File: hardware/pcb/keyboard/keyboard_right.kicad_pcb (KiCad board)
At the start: 2 copper layers, 133.8 x 110.4 mm, 108 parts, among them J1 SM04B-SRSS-TB, J2 PJ320D, J3 HRO_TYPE-C-31-M-12, J4 FH34SRJ-10S-0.5SH, SW29 PTS845, U1 74HC4051, U2 OPA350UA, U3 DT1446-04S, U4 XC6220B331MR-G, U5 STM32G0B1KETx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

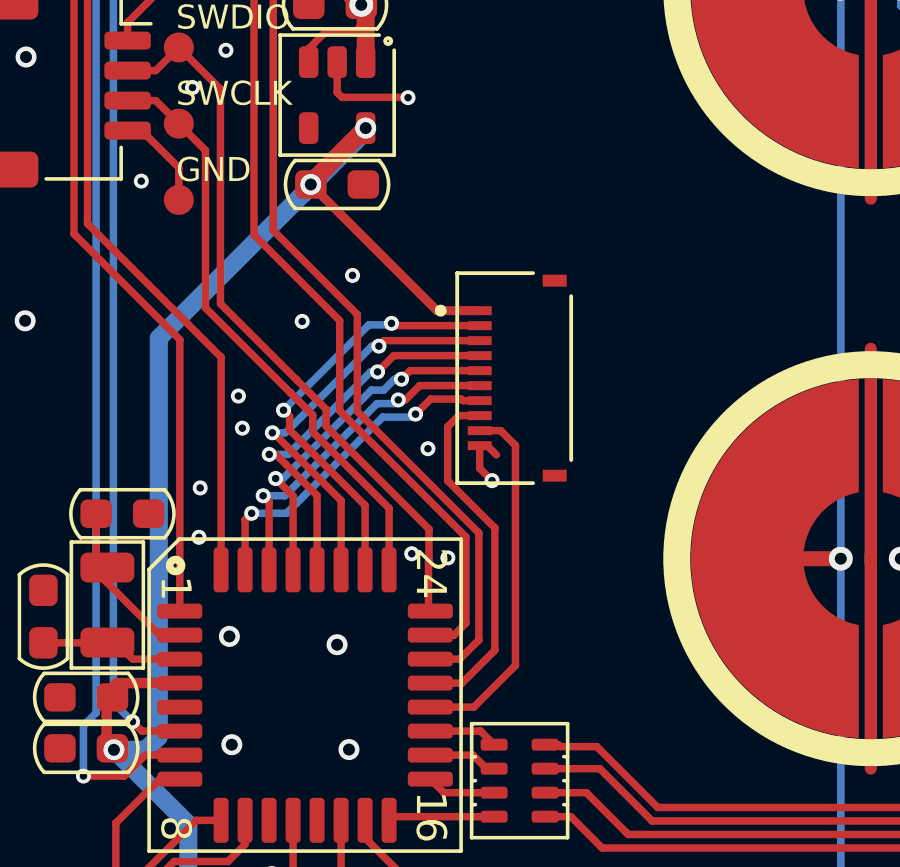
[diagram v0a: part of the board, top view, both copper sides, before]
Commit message: roate FFC Connector
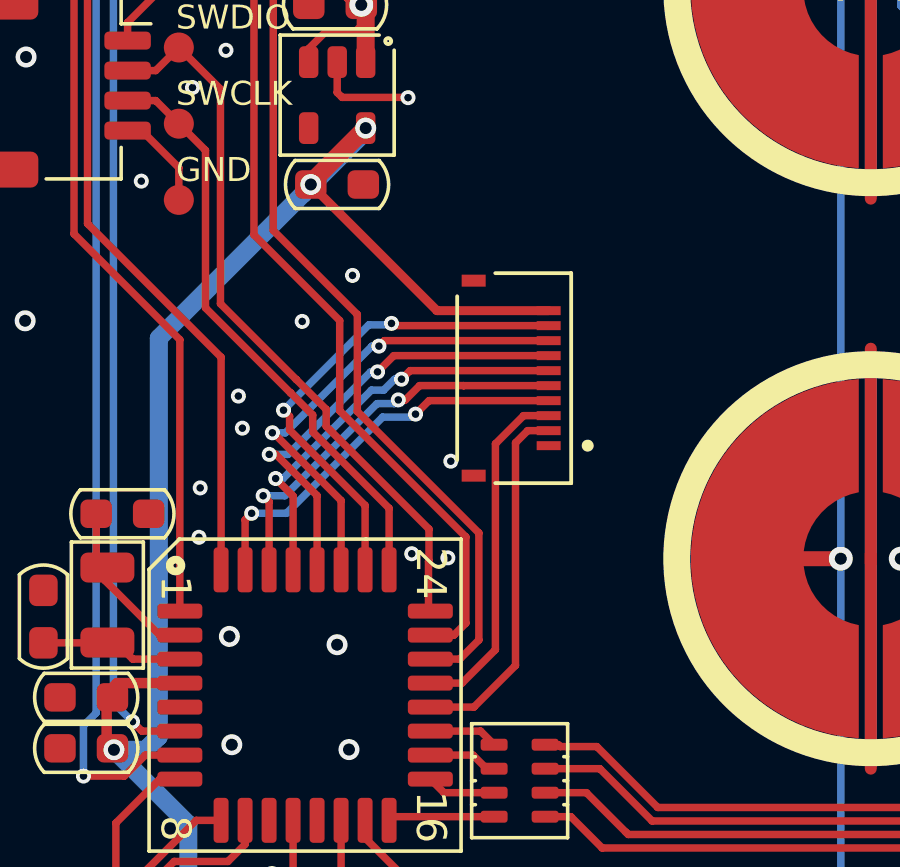
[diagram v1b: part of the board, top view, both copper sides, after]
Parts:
- turned J4 to -90 degrees
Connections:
- J4 pad 1: +3V3 -> GND
- J4 pad 10: GND -> +3V3
- J4 pad 2: ACCS_1 -> ACCS_8
- J4 pad 3: ACCS_2 -> ACCS_7
- J4 pad 4: ACCS_3 -> ACCS_6
- J4 pad 5: ACCS_4 -> ACCS_5
- J4 pad 6: ACCS_5 -> ACCS_4
- J4 pad 7: ACCS_6 -> ACCS_3
- J4 pad 8: ACCS_7 -> ACCS_2
- J4 pad 9: ACCS_8 -> ACCS_1
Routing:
- net ACCS_5: track 11.3 -> 13.6 mm
- net ACCS_4: track 11.6 -> 13.9 mm
- net ACCS_1: track 14.2 -> 16.5 mm
- net +3V3: track 68.9 -> 71.2 mm
- net ACCS_2: track 13.7 -> 16.0 mm
- net ACCS_3: track 13.0 -> 15.3 mm
- net ACCS_6: track 11.2 -> 13.4 mm
- net GND: track 15.1 -> 13.3 mm, vias 45 -> 44

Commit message: Right init
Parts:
- removed R4: 10k, PCM_Resistor_SMD_AKL:R_0603_1608Metric_Pad0.98x0.95mm
- removed R5: 5.6k, PCM_Resistor_SMD_AKL:R_0603_1608Metric_Pad0.98x0.95mm
- added C11: 4.7 uF, PCM_Capacitor_SMD_AKL:C_0603_1608Metric, F.Cu at (86.5, 89.7)
- added C12: 1u, PCM_Capacitor_SMD_AKL:C_0603_1608Metric, F.Cu at (85.4, 91.6)
- added C13: 10n, PCM_Capacitor_SMD_AKL:C_0603_1608Metric, F.Cu at (85.4, 94.0)
- added FB1: 1kΩ 100mhz, Inductor_SMD:L_0603_1608Metric, F.Cu at (87.7, 92.3)
- added R1: 10k, PCM_Resistor_SMD_AKL:R_0603_1608Metric, F.Cu at (74.5, 85.7)
- C10, C2, C3, C4, C6, C7: footprint PCM_Capacitor_SMD_AKL:C_0603_1608Metric_Pad1.05x0.95mm -> PCM_Capacitor_SMD_AKL:C_0603_1608Metric
- C5: value 4.7u -> 0.1uF; footprint PCM_Capacitor_SMD_AKL:C_0603_1608Metric_Pad1.05x0.95mm -> PCM_Capacitor_SMD_AKL:C_0603_1608Metric
- G19, H13, H14, H15, H16: moved to B.Cu
- J4: value FH34SRJ-10S-0.5SH -> Conn_01x12_MountingPin; footprint ec_parts:HRS_FH34SRJ-10S-0.5SH(50) -> ec_parts:HRS_FH34SRJ-12S-0.5SH(50)
- R6, R7: footprint PCM_Resistor_SMD_AKL:R_0603_1608Metric_Pad0.98x0.95mm -> PCM_Resistor_SMD_AKL:R_0603_1608Metric
- U5: value STM32G0B1KETx -> STM32G431KBTx; footprint PCM_Package_QFP_AKL:LQFP-32_7x7mm_P0.8mm -> Package_QFP:LQFP-32_7x7mm_P0.8mm
- Y1: value 32.768kHz -> 8MHz; footprint PCM_Crystal_AKL:Crystal_SMD_3215-2Pin_3.2x1.5mm -> PCM_Crystal_Handsoldering_AKL:Crystal_SMD_2520-4Pin_2.5x2.0mm
- moved H16 17.2 mm to (72.5, 102.7)
- moved H13 17.1 mm to (88.2, 102.7)
- moved H15 16.8 mm to (72.5, 55.6)
- moved H14 16.7 mm to (88.2, 55.6)
- moved C7 9.48 mm to (72.8, 85.7), turned to 90 degrees
- moved C6 7.28 mm to (73.8, 80.0), turned to 0 degrees
- moved C2 6.68 mm to (77.3, 93.1)
- moved C3 6.68 mm to (75.2, 108.1)
- moved H12 6.68 mm to (110.0, 129.2)
- moved C9 6.68 mm to (82.2, 68.5), turned to 180 degrees
- moved F1 6.68 mm to (86.2, 43.5)
- moved J1 6.68 mm to (73.2, 65.2)
- moved L1 6.68 mm to (86.4, 40.8)
- moved SW5 6.68 mm to (176.0, 64.4)
- moved TP1 6.68 mm to (76.9, 61.4)
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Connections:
- C6 pad 2: /OSC32_IN -> Net-(U5-PF0)
- C7 pad 2: /OSC32_OUT -> Net-(U5-PF1)
- D1 pad 2: Net-(D1-A) -> VBUS
- F1 pad 1: Net-(D1-A) -> VBUS
- F1 pad 2: VBUS -> Net-(F1-Pad2)
- J1 pad 1: +5V -> +3V3
- J3 pad A4: VBUS -> Net-(F1-Pad2)
- J3 pad A9: VBUS -> Net-(F1-Pad2)
- J3 pad B4: VBUS -> Net-(F1-Pad2)
- J3 pad B9: VBUS -> Net-(F1-Pad2)
- J4 pad 10: +3V3 -> unconnected-(J4-Pin_10-Pad10)
- J4 pad 2: ACCS_8 -> ACCS_7
- J4 pad 3: ACCS_7 -> ACCS_6
- J4 pad 4: ACCS_6 -> ACCS_5
- J4 pad 5: ACCS_5 -> ACCS_4
- J4 pad 6: ACCS_4 -> ACCS_3
- J4 pad 7: ACCS_3 -> ACCS_2
- J4 pad 8: ACCS_2 -> ACCS_1
- J4 pad 9: ACCS_1 -> +3V3
- TP1 pad 1: +5V -> +3V3
- U5 pad 1: USART_RX -> +3V3
- U5 pad 10: CSEL2 -> CSEL1
- U5 pad 11: /ADC1_IN4 -> CSEL2
- U5 pad 13: /ADC1_IN6 -> CHARGE_RST
- U5 pad 14: CHARGE_RST -> GND
- U5 pad 15: CSEL_EN -> VDDA
- U5 pad 16: TX3 -> GND
- U5 pad 17: TX2 -> +3V3
- U5 pad 18: TX1 -> TX3
- U5 pad 19: TX0 -> TX2
- U5 pad 2: /OSC32_IN -> Net-(U5-PF0)
- U5 pad 20: ACCS_8 -> TX1
- U5 pad 21: ACCS_7 -> D-
- U5 pad 22: D- -> D+
- U5 pad 23: D+ -> SWDIO
- U5 pad 24: SWDIO -> SWCLK
- U5 pad 25: SWCLK -> TX0
- U5 pad 26: ACCS_1 -> ACCS_2
- U5 pad 27: ACCS_2 -> ACCS_3
- U5 pad 28: ACCS_3 -> ACCS_4
- U5 pad 29: ACCS_4 -> ACCS_5
- U5 pad 3: /OSC32_OUT -> Net-(U5-PF1)
- U5 pad 30: ACCS_5 -> ACCS_6
- U5 pad 31: ACCS_6 -> ACCS_7
- U5 pad 32: USART_TX -> GND
- U5 pad 4: +3V3 -> /NRST
- U5 pad 5: GND -> ACCS_1
- U5 pad 6: /NRST -> CSEL_EN
- U5 pad 7: VBUS_DEC -> USART_TX
- U5 pad 8: CSEL0 -> USART_RX
- U5 pad 9: CSEL1 -> CSEL0
- Y1 pad 1: /OSC32_IN -> Net-(U5-PF1)
- Y1 pad 2: /OSC32_OUT -> GND
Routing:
- net VBUS_DEC: track 52.9 -> 0.00 mm, vias 4 -> 0
- net +3V3: track 71.2 -> 109.9 mm, vias 5 -> 9
- net GND: track 13.3 -> 33.4 mm, vias 44 -> 38
- net Net-(F1-Pad2): track 0.00 -> 17.2 mm, vias 0 -> 2
- net ACCS_8: track 12.7 -> 0.00 mm
- net VBUS: track 17.2 -> 29.5 mm, vias 2 -> 0
- net CSEL_EN: track 17.3 -> 29.0 mm, vias 0 -> 2
- net +5V: track 38.3 -> 27.5 mm, vias 2 -> 0
- net VDDA: track 0.00 -> 6.74 mm
- net Net-(U5-PF1): track 0.00 -> 5.62 mm
- net ACCS_1: track 16.5 -> 22.0 mm
- net USART_RX: track 40.8 -> 45.5 mm, vias 0 -> 2
- net ACCS_2: track 16.0 -> 11.4 mm
- net /OSC32_IN: track 4.50 -> 0.00 mm
- net Net-(D1-A): track 4.46 -> 0.00 mm
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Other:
- outline, holes or cut-outs redrawn
- board text added: "SWC"
- board text added: "SWD"
- board text removed: "SWCLK"
- board text removed: "SWDIO"

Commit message: usb hib init
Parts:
- added R4: 10k, PCM_Resistor_SMD_AKL:R_0603_1608Metric, F.Cu at (87.8, 66.9)
- added R5: 5.1k, PCM_Resistor_SMD_AKL:R_0603_1608Metric, F.Cu at (87.8, 65.1)
- added R8: 1k, PCM_Resistor_SMD_AKL:R_0603_1608Metric, F.Cu at (87.8, 68.6)
- J4: value Conn_01x12_MountingPin -> HRS_FH34SRJ-12S-0.5SH_50_
- moved H14 0.41 mm to (88.2, 55.2)
- moved H15 0.41 mm to (72.5, 55.2)
- moved C8 0.25 mm to (82.4, 62.5)
- moved C9 0.19 mm to (82.4, 68.5)
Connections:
- U5 pad 5: ACCS_1 -> CSEL0
- U5 pad 9: CSEL0 -> ACCS_1
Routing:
- net ACCS_3: track 11.9 -> 23.2 mm
- net ACCS_1: track 22.0 -> 33.3 mm
- net CSEL_EN: track 29.0 -> 24.4 mm
- net CSEL0: track 20.3 -> 22.6 mm
- net GND: track 33.4 -> 31.2 mm
- net +3V3: track 109.9 -> 110.9 mm, vias 9 -> 10

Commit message: preproduction
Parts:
- J4: value HRS_FH34SRJ-12S-0.5SH_50_ -> HRS_FH34SRJ-12S-0.5SH(50)
- U3: value DT1446-04S -> PRTR5V0U2X; footprint PCM_Package_TO_SOT_SMD_AKL:SOT-363_SC-70-6_Handsoldering -> PCM_Package_TO_SOT_SMD_AKL:SOT-143
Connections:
- U3 pad 1: USART_RX -> GND
- U3 pad 2: GND -> D+
- U3 pad 3: D+ -> D-
- U3 pad 4: D- -> +5V
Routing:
- net GND: track 31.2 -> 25.4 mm, vias 38 -> 40
- net USART_TX: track 45.2 -> 43.2 mm
- net +5V: track 27.6 -> 29.4 mm
- net D+: track 53.9 -> 52.9 mm
- net USART_RX: track 45.5 -> 44.9 mm
- net D-: track 54.3 -> 53.7 mm

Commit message: temp
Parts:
- C1, C8, C9: footprint PCM_Capacitor_SMD_AKL:C_0603_1608Metric_Pad1.05x0.95mm -> PCM_Capacitor_SMD_AKL:C_0603_1608Metric
- C6, C7: value 22p -> 10pF
- R2, R3: footprint PCM_Resistor_SMD_AKL:R_0603_1608Metric_Pad0.98x0.95mm -> PCM_Resistor_SMD_AKL:R_0603_1608Metric
- RN1, RN2: value 1k R_Array_Concave_4x0603 -> 100k R_Array_Concave_4x0603
- Y1: value 8MHz -> 8MHz 10pF

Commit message: rev2
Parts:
- added R9: 1k, PCM_Resistor_SMD_AKL:R_0603_1608Metric, F.Cu at (88.9, 80.3)
- J1: footprint Connector_JST:JST_SH_SM04B-SRSS-TB_1x04-1MP_P1.00mm_Horizontal -> Connector_JST:JST_SH_SM03B-SRSS-TB_1x03-1MP_P1.00mm_Horizontal
- J4: value HRS_FH34SRJ-12S-0.5SH(50) -> HRS_FH34SRJ-12S-0.5SH_50_
- moved R4 1.91 mm to (87.8, 65.0)
- moved R5 1.60 mm to (87.8, 66.7), turned to 180 degrees
- moved R8 1.11 mm to (88.7, 69.3)
- moved J1 0.50 mm to (73.2, 65.7)
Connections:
- J1 pad 1: +3V3 -> SWCLK
- J1 pad 2: SWDIO -> GND
- J1 pad 3: SWCLK -> SWDIO
- J1 pad MP: GND -> unconnected-(J1-MountPin-PadMP)
- J4 pad 10: unconnected-(J4-Pin_10-Pad10) -> +5V
- J4 pad 11: unconnected-(J4-Pin_11-Pad11) -> +5V
- J4 pad 12: VBUS -> unconnected-(J4-Pin_12-Pad12)
- J4 pad 4: ACCS_5 -> GND
- J4 pad 9: +3V3 -> unconnected-(J4-Pin_9-Pad9)
- R4 pad 1: ACCS_3 -> PB6
- R5 pad 2: ACCS_3 -> PB6
- R8 pad 1: ACCS_1 -> ACCS_4
- R8 pad 2: +3V3 -> ACCS_1
- TP1 pad 2: SWDIO -> SWCLK
- TP1 pad 3: SWCLK -> GND
- TP1 pad 4: GND -> SWDIO
- U5 pad 29: ACCS_5 -> PB6
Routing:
- net PB6: track 0.00 -> 19.8 mm, vias 0 -> 4
- net ACCS_5: track 12.5 -> 0.00 mm, vias 2 -> 0
- net +5V: track 29.4 -> 41.5 mm
- net ACCS_3: track 23.2 -> 11.9 mm
- net GND: track 25.4 -> 16.7 mm, vias 40 -> 27
- net +3V3: track 110.9 -> 102.8 mm
- net VBUS: track 29.6 -> 21.8 mm
- net ACCS_4: track 12.1 -> 19.0 mm
- net ACCS_6: track 13.9 -> 20.0 mm
- net ACCS_7: track 15.1 -> 19.4 mm
- net SWDIO: track 26.5 -> 22.4 mm
- net SWCLK: track 22.0 -> 25.9 mm
- net ACCS_1: track 33.3 -> 31.0 mm, vias 2 -> 3

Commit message: rev2 pre production
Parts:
- J4: value HRS_FH34SRJ-12S-0.5SH_50_ -> HRS_FH34SRJ-12S-0.5SH(50)
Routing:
- net GND: track 16.7 -> 38.2 mm, vias 27 -> 30
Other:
- board text added: "PA4/PB5"
- board text added: "PB7/PB8"

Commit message: init memory
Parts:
- removed R9: 1k, PCM_Resistor_SMD_AKL:R_0603_1608Metric
- added C14: 10n, PCM_Capacitor_SMD_AKL:C_0603_1608Metric, F.Cu at (72.9, 74.3)
- added H18: ~, ec_parts:SMT-SO-M1.6-screwhole_only, F.Cu at (72.5, 71.2)
- added H19: ~, ec_parts:SMT-SO-M1.6-screwhole_only, F.Cu at (88.2, 71.2)
- added U6: 24FC01T-I/OT, ec_parts:SOT-23-5_2P9X1P6_MCH, F.Cu at (73.8, 76.9)
- J4: value HRS_FH34SRJ-12S-0.5SH(50) -> HRS_FH34SRJ-06S-0.5SH(50); footprint ec_parts:HRS_FH34SRJ-12S-0.5SH(50) -> ec_parts:CONN6x1_FH34SRJ-6S-0.5SH50_HIR
- moved R8 13.5 mm to (76.1, 74.3), turned to 0 degrees
- moved J4 7.89 mm to (80.5, 76.5), turned to 0 degrees
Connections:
- C13 pad 1: VDDA -> unconnected-(C13-Pad1)
- C13 pad 2: GND -> unconnected-(C13-Pad2)
- J4 pad 2: ACCS_7 -> ACCS_4
- J4 pad 3: ACCS_6 -> ACCS_3
- J4 pad 4: GND -> ACCS_2
- J4 pad 5: ACCS_4 -> ACCS_1
- J4 pad 6: ACCS_3 -> +3V3
- SW29 pad MP: (no net) -> unconnected-(SW29-PadMP)_1
- U5 pad 30: ACCS_6 -> I2C1_SDA
- U5 pad 31: ACCS_7 -> I2C1_SCL
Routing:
- net ACCS_6: track 20.0 -> 0.00 mm, vias 2 -> 0
- net ACCS_7: track 19.4 -> 0.00 mm, vias 2 -> 0
- net +5V: track 41.5 -> 29.4 mm
- net ACCS_1: track 31.0 -> 20.9 mm
- net I2C1_SDA: track 0.00 -> 9.78 mm
- net +3V3: track 102.8 -> 110.8 mm
- net I2C1_SCL: track 0.00 -> 7.72 mm
- net ACCS_4: track 19.0 -> 13.0 mm
- net ACCS_3: track 11.9 -> 6.74 mm, vias 2 -> 0
- net GND: track 38.2 -> 42.7 mm
- net ACCS_2: track 11.4 -> 7.77 mm, vias 2 -> 0
- net SWCLK: track 25.9 -> 27.7 mm
- net Net-(U6-VCC): track 0.00 -> 1.64 mm
- net PB6: track 19.8 -> 19.0 mm, vias 4 -> 2
- net SWDIO: track 22.4 -> 23.1 mm
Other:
- board text removed: "PA4/PB5"
- board text removed: "PB7/PB8"
